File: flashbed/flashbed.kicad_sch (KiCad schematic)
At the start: 47 parts, among them J1 , J2 , J3 , J4 , SW1 SW_Push

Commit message: Cập nhật file PCB
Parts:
- J4: footprint Connector_IDC:IDC-Header_2x05_P2.54mm_Vertical -> Connector_IDC:IDC-Header_2x05_P2.54mm_Horizontal
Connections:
- net RST: now reaches J2.4 (Pin_4), SW1.2
- net RST: now also J4.1 (Pin_1)
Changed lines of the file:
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@@
 (kicad_sch (version 20211123) (generator eeschema)
   (paper "A4")
+  (junction (at 128.27 54.61) (diameter 0) (color 0 0 0 0)
+  )
   (wire (pts (xy 128.27 67.31) (xy 124.46 67.31))
     (stroke (width 0) (type default) (color 0 0 0 0))
@@
   (wire (pts (xy 119.38 72.39) (xy 116.84 72.39))
     (stroke (width 0) (type default) (color 0 0 0 0))
+  )
+  (wire (pts (xy 128.27 54.61) (xy 146.05 54.61))
+    (stroke (width 0) (type default) (color 0 0 0 0))
+  )
+  (global_label "RST" (shape input) (at 210.82 58.42 180) (fields_autoplaced)
+    (effects (font (size 1.27 1.27)) (justify right))
+    (property "Intersheet References" "${INTERSHEET_REFS}" (id 0) (at 204.9598 58.4994 0)
+      (effects (font (size 1.27 1.27)) (justify right) hide)
+    )
   )
   (global_label "SWCLK" (shape input) (at 223.52 58.42 0) (fields_autoplaced)
@@
     (effects (font (size 1.27 1.27)) (justify left))
     (property "Intersheet References" "${INTERSHEET_REFS}" (id 0) (at 231.7993 60.8806 0)
+      (effects (font (size 1.27 1.27)) (justify left) hide)
+    )
+  )
+  (global_label "RST" (shape input) (at 146.05 54.61 0) (fields_autoplaced)
+    (effects (font (size 1.27 1.27)) (justify left))
+    (property "Intersheet References" "${INTERSHEET_REFS}" (id 0) (at 151.9102 54.5306 0)
       (effects (font (size 1.27 1.27)) (justify left) hide)
     )
@@
     (property "Reference" "J4" (id 0) (at 217.17 52.07 0))
     (property "Value" " " (id 1) (at 217.17 54.61 0))
-    (property "Footprint" "Connector_IDC:IDC-Header_2x05_P2.54mm_Vertical" (id 2) (at 215.9 63.5 0)
+    (property "Footprint" "Connector_IDC:IDC-Header_2x05_P2.54mm_Horizontal" (id 2) (at 215.9 63.5 0)
       (effects (font (size 1.27 1.27)) hide)
     )
@@
     (in_bom yes) (on_board yes)
     (property "Reference" "D10" (id 0) (at 111.76 55.88 0))
-    (property "Value" "VCC" (id 1) (at 114.3635 53.34 0))
+    (property "Value" "VCC" (id 1) (at 114.3 53.34 0))
     (property "Footprint" "Library:LED_0603_1608Metric_Pad1.05x0.95mm_HandSolder" (id 2) (at 114.3 57.15 90)
       (effects (font (size 1.27 1.27)) hide)
@@
     )
     (path "/81cded2c-b3bc-49d6-b551-c4bbd6efa871"
-      (reference "J4") (unit 1) (value " ") (footprint "Connector_IDC:IDC-Header_2x05_P2.54mm_Vertical")
+      (reference "J4") (unit 1) (value " ") (footprint "Connector_IDC:IDC-Header_2x05_P2.54mm_Horizontal")
     )
     (path "/06bc45b1-e570-4fb7-be3c-96827dc840b0"

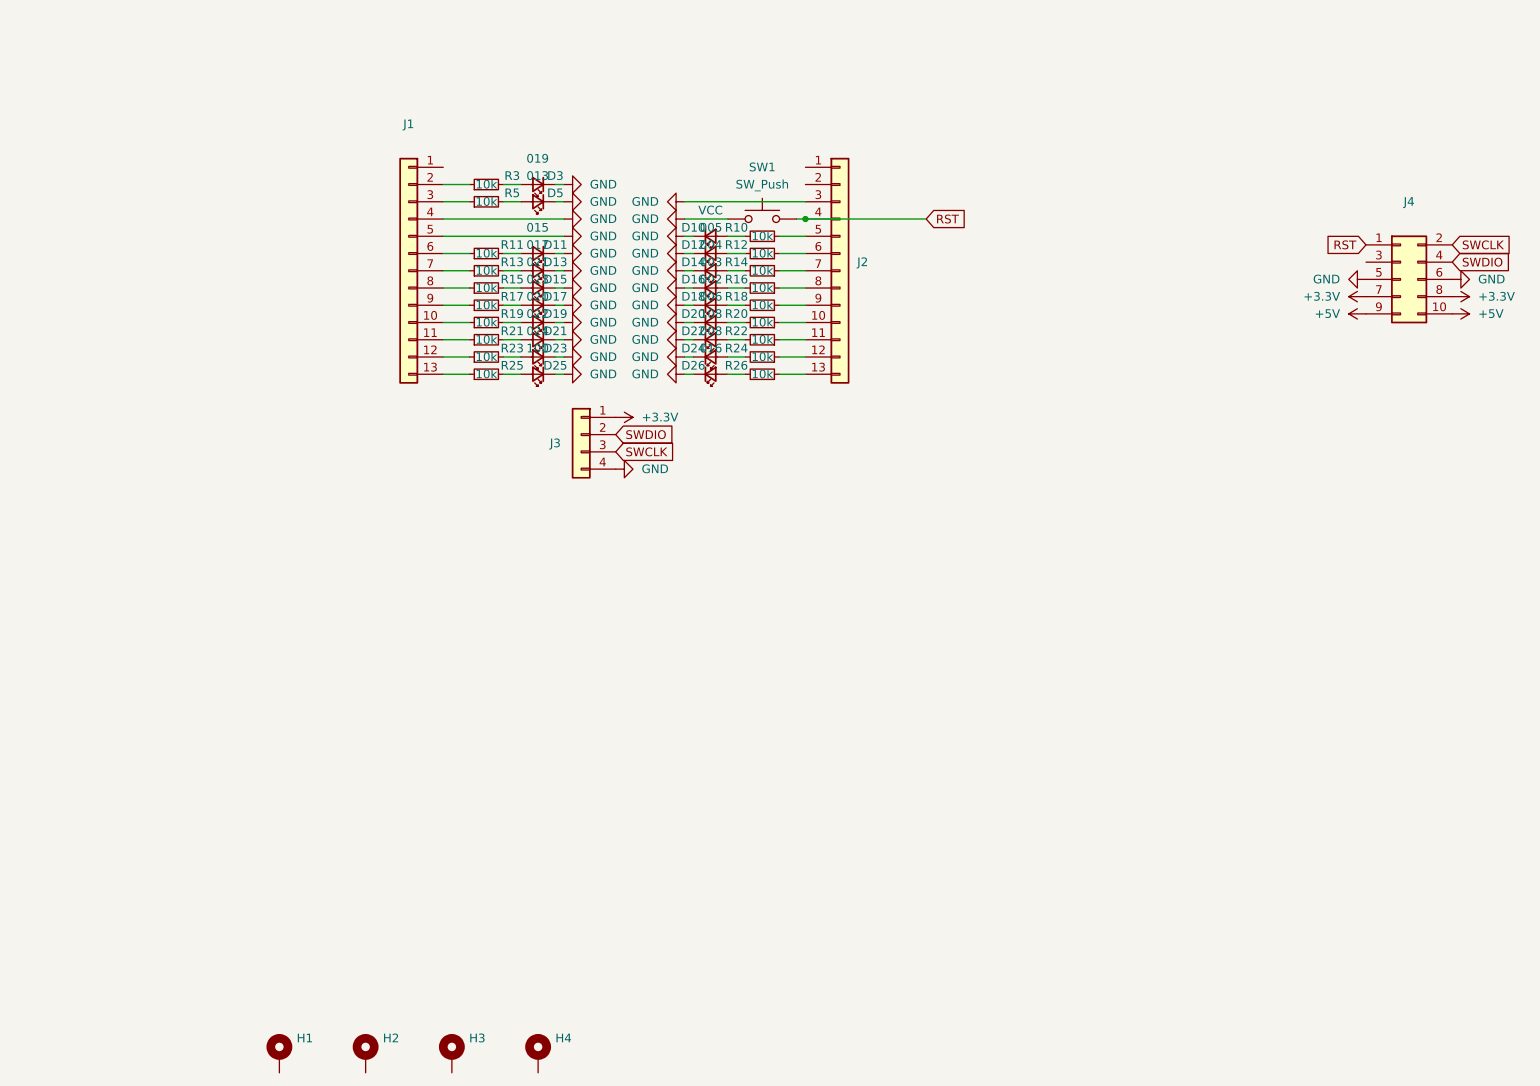
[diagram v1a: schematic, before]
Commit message: Cập nhật: - Thêm flashbed cho nrfpill - Thay đổi GPIO Kimiro
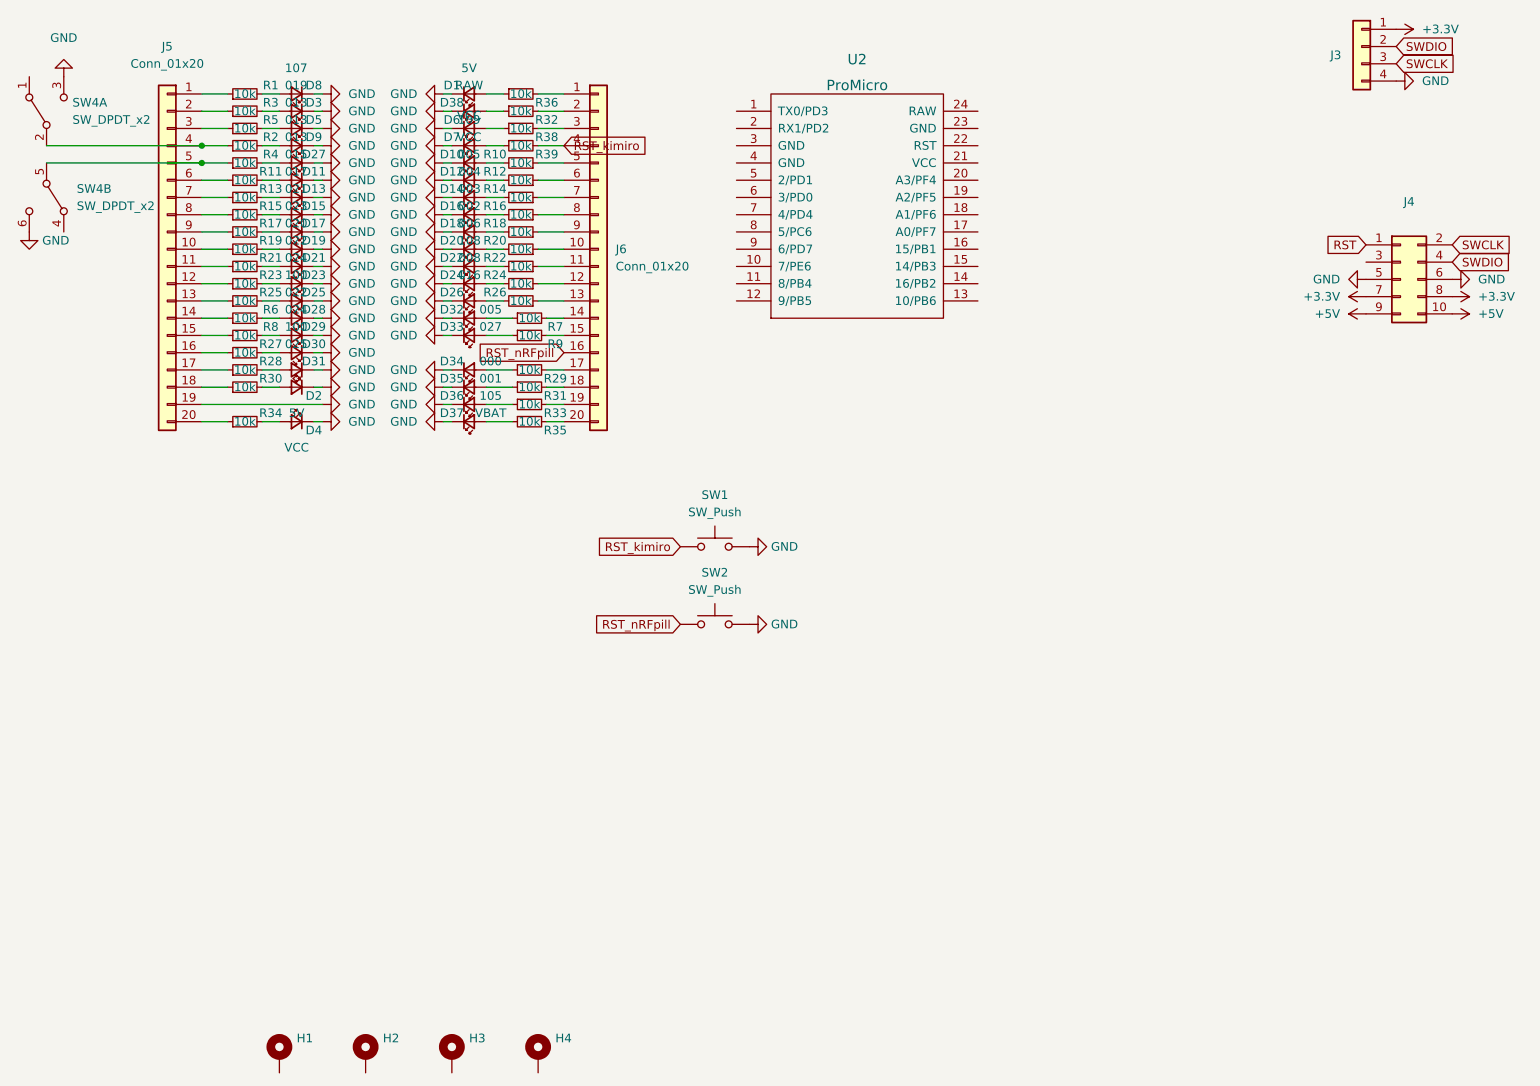
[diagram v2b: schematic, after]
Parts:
- removed J1, J2: (no value), Library:PinHeader_1x13_P2.54mm_Vertical, symbol Connector_Generic:Conn_01x13
- added D1, D2: 5V, Library:LED_0603_1608Metric_Pad1.05x0.95mm_HandSolder, symbol Device:LED_Small
- added D27, D9: 013, Library:LED_0603_1608Metric_Pad1.05x0.95mm_HandSolder, symbol Device:LED_Small
- added D28: 022, Library:LED_0603_1608Metric_Pad1.05x0.95mm_HandSolder, symbol Device:LED_Small
- added D29: 024, Library:LED_0603_1608Metric_Pad1.05x0.95mm_HandSolder, symbol Device:LED_Small
- added D30: 100, Library:LED_0603_1608Metric_Pad1.05x0.95mm_HandSolder, symbol Device:LED_Small
- added D31: 025, Library:LED_0603_1608Metric_Pad1.05x0.95mm_HandSolder, symbol Device:LED_Small
- added D32: 005, Library:LED_0603_1608Metric_Pad1.05x0.95mm_HandSolder, symbol Device:LED_Small
- added D33: 027, Library:LED_0603_1608Metric_Pad1.05x0.95mm_HandSolder, symbol Device:LED_Small
- added D34: 000, Library:LED_0603_1608Metric_Pad1.05x0.95mm_HandSolder, symbol Device:LED_Small
- added D35: 001, Library:LED_0603_1608Metric_Pad1.05x0.95mm_HandSolder, symbol Device:LED_Small
- added D36: 105, Library:LED_0603_1608Metric_Pad1.05x0.95mm_HandSolder, symbol Device:LED_Small
- added D37: VBAT, Library:LED_0603_1608Metric_Pad1.05x0.95mm_HandSolder, symbol Device:LED_Small
- added D38: RAW, Library:LED_0603_1608Metric_Pad1.05x0.95mm_HandSolder, symbol Device:LED_Small
- added D4, D6: VCC, Library:LED_0603_1608Metric_Pad1.05x0.95mm_HandSolder, symbol Device:LED_Small
- added D7: 109, Library:LED_0603_1608Metric_Pad1.05x0.95mm_HandSolder, symbol Device:LED_Small
- added D8: 107, Library:LED_0603_1608Metric_Pad1.05x0.95mm_HandSolder, symbol Device:LED_Small
- added J5, J6: Conn_01x20, Library:PinHeader_1x20_P2.54mm_Vertical, symbol Connector_Generic:Conn_01x20
- added R1, R2, R27, R28, R29, R30, R31, R32, R33, R34, R35, R36, R38, R39, R4, R6, R7, R8, R9: 10k, Library:R_0603_1608Metric_Pad0.98x0.95mm_HandSolder, symbol Device:R_Small
- added SW2: SW_Push, Button_Switch_SMD:SW_SPST_TL3342, symbol Switch:SW_Push
- added SW4: SW_DPDT_x2, symbol Switch:SW_DPDT_x2
- added U2: ProMicro, symbol keebio:ProMicro
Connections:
- net GND: now also SW1.2, D1.1 (K), D2.1 (K), D27.1 (K), D28.1 (K), D29.1 (K), D30.1 (K), D31.1 (K), D32.1 (K), D33.1 (K), D34.1 (K), D35.1 (K), D36.1 (K), D37.1 (K), D38.1 (K), D4.1 (K), D6.1 (K), D7.1 (K), D8.1 (K), D9.1 (K), J5.19 (Pin_19), SW2.2, SW4.3 (C), SW4.6 (C); no longer SW1.1
- net RST: no longer SW1.2
- net at R26.1: now also J6.13 (Pin_13)
- net at R3.1: now also J5.2 (Pin_2)
- net at R12.1: now also J6.6 (Pin_6)
- net at R5.1: now also J5.3 (Pin_3)
- net at R22.1: now also J6.11 (Pin_11)
- net at R23.1: now also J5.12 (Pin_12)
- net at R24.1: now also J6.12 (Pin_12)
- net at R14.1: now also J6.7 (Pin_7)
- net at R17.1: now also J5.9 (Pin_9)
- net at R19.1: now also J5.10 (Pin_10)
- net at R21.1: now also J5.11 (Pin_11)
- net at R25.1: now also J5.13 (Pin_13)
- net at R11.1: now also J5.6 (Pin_6)
- net at R13.1: now also J5.7 (Pin_7)
- net at R15.1: now also J5.8 (Pin_8)
- net at R20.1: now also J6.10 (Pin_10)
- net at R10.1: now also J6.5 (Pin_5)
- net at R18.1: now also J6.9 (Pin_9)
- net at R16.1: now also J6.8 (Pin_8)
- new net: D6.2 (A), R38.1
- new net: J6.3 (Pin_3), R38.2
- new net: D35.2 (A), R31.1
- new net: J6.18 (Pin_18), R31.2
- new net: D30.2 (A), R27.2
- new net: J5.15 (Pin_15), R8.1
- new net: D29.2 (A), R8.2
- new net: J5.5 (Pin_5), R4.1, SW4.5 (B)
- new net: D33.2 (A), R9.1
- new net: J6.15 (Pin_15), R9.2
- new net: J5.14 (Pin_14), R6.1
- new net: D28.2 (A), R6.2
- new net: D32.2 (A), R7.1
- new net: D34.2 (A), R29.1
- new net: D4.2 (A), R34.2
- new net: D2.2 (A), R30.2
- new net: D36.2 (A), R33.1
- new net: J5.20 (Pin_20), R34.1
- new net: D38.2 (A), R32.1
- new net: J5.4 (Pin_4), R2.1, SW4.2 (B)
- new net: J6.14 (Pin_14), R7.2
- new net: J6.2 (Pin_2), R32.2
- new net: J5.17 (Pin_17), R28.1
- new net: D31.2 (A), R28.2
- new net: J6.19 (Pin_19), R33.2
- new net: J5.1 (Pin_1), R1.1
- new net: D8.2 (A), R1.2
- new net: J5.18 (Pin_18), R30.1
- new net: D37.2 (A), R35.1
- new net: J6.20 (Pin_20), R35.2
- new net: D1.2 (A), R36.1
- new net: D9.2 (A), R2.2
- new net: J6.1 (Pin_1), R36.2
- new net: J6.17 (Pin_17), R29.2
- new net: D7.2 (A), R39.1
- new net: J5.16 (Pin_16), R27.1
- new net: D27.2 (A), R4.2
- new net RST_kimiro: J6.4 (Pin_4), R39.2, SW1.1
- new net RST_nRFpill: J6.16 (Pin_16), SW2.1
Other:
- moved on the sheet: D10, D11, D12, D13, D14, D15, D16, D17, D18, D19, D20, D21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

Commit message: Cap nhat
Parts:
- removed U2: ProMicro, symbol keebio:ProMicro
- added J2: (no value), Library:PinHeader_1x04_P2.54mm_Vertical, symbol Connector_Generic:Conn_01x04
- renumbered D8 to D1, D1 to D2, D28 to D27, D32 to D28, D33 to D30, D30 to D31, D31 to D32, D34 to D33, D2 to D34, D4 to D37, D37 to D38, D38 to D4, D9 to D7, D7 to D8, D27 to D9, J3 to J1, J5 to J3, J6 to J4, J4 to J5, R36 to R2, R6 to R27, R7 to R28, R8 to R29, R9 to R30, R27 to R31, R28 to R32, R29 to R33, R30 to R34, R31 to R35, R33 to R36, R34 to R37, R35 to R38, R32 to R4, R38 to R6, R2 to R7, R39 to R8, R4 to R9, SW4 to SW1, SW1 to SW2, SW2 to SW3
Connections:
- net +5V: now also J3.18 (Pin_18), R34.1
- net SWCLK: now also J2.3 (Pin_3)
- net SWDIO: now also J2.2 (Pin_2)
